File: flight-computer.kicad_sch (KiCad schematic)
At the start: 42 parts, among them J1 MicroSD Slot, J2 USB_C_Receptacle_USB2.0_16P, SW1 SW_Push, SW2 SW_Push, U1 RP2040, U2 W25Q16JVSS, U3 USBLC6-2SC6, Y1 12MHz

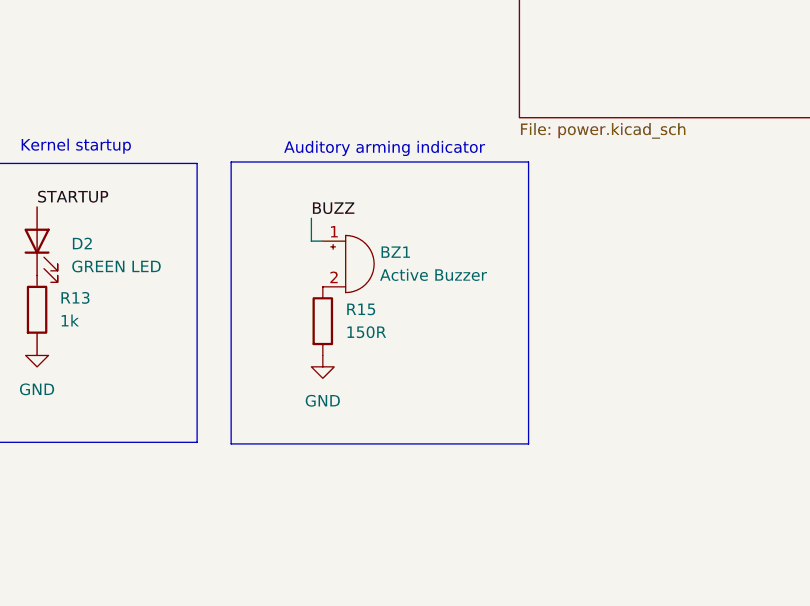
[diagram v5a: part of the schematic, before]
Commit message: Updated PCB so components are now on there.
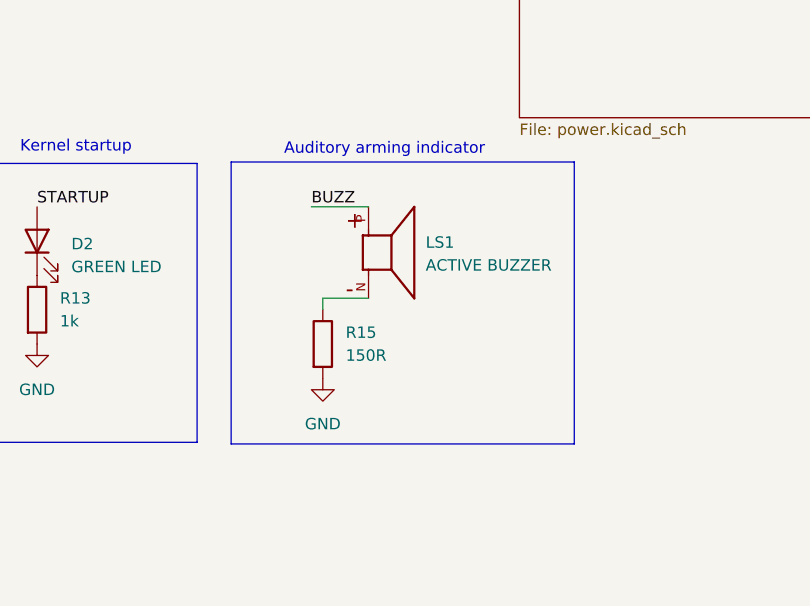
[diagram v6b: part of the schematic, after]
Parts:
- removed BZ1: Active Buzzer, buzzer:XDCR_AI-1223-TWT-3V-2-R, symbol Device:Buzzer
- added LS1: ACTIVE BUZZER, buzzer:XDCR_AI-1223-TWT-3V-2-R, symbol AI-1223-TWT-3V-2-R:AI-1223-TWT-3V-2-R
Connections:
- net BUZZ: now also LS1.P
- net at R15.1: now also LS1.N
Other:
- moved on the sheet: R15
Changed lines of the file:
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@@
 	(wire
 		(pts
+			(xy 322.58 234.95) (xy 317.5 234.95)
+		)
+		(stroke
+			(width 0)
+			(type default)
+		)
+	)
+	(wire
+		(pts
 			(xy 39.37 143.51) (xy 50.8 143.51)
 		)
@@
 	(wire
 		(pts
-			(xy 316.23 226.06) (xy 316.23 228.6)
-		)
-		(stroke
-			(width 0)
-			(type default)
-		)
-	)
-	(wire
-		(pts
 			(xy 72.39 125.73) (xy 60.96 125.73)
 		)
@@
 	(wire
 		(pts
+			(xy 317.5 234.95) (xy 317.5 236.22)
+		)
+		(stroke
+			(width 0)
+			(type default)
+		)
+	)
+	(wire
+		(pts
 			(xy 278.13 68.58) (xy 266.7 68.58)
 		)
@@
 	(wire
 		(pts
-			(xy 316.23 228.6) (xy 317.5 228.6)
+			(xy 316.23 224.79) (xy 322.58 224.79)
 		)
 		(stroke
@@
 	(rectangle
 		(start 307.3134 219.8042)
-		(end 340.36 251.1317)
+		(end 345.44 251.1317)
 		(stroke
 			(width 0)
@@
 	)
 	(label "BUZZ"
-		(at 316.23 226.06 0)
+		(at 316.23 224.79 0)
 		(fields_autoplaced yes)
 		(effects
@@
 	(symbol
 		(lib_id "power:GND")
-		(at 317.5 241.3 0)
+		(at 317.5 243.84 0)
 		(unit 1)
 		(exclude_from_sim no)
@@
 		(fields_autoplaced yes)
 		(property "Reference" "#PWR037"
-			(at 317.5 247.65 0)
+			(at 317.5 250.19 0)
 			(effects
 				(font
@@
 		)
 		(property "Value" "GND"
-			(at 317.5 246.38 0)
+			(at 317.5 248.92 0)
 			(effects
 				(font
@@
 		)
 		(property "Footprint" ""
-			(at 317.5 241.3 0)
+			(at 317.5 243.84 0)
 			(effects
 				(font
@@
 		)
 		(property "Datasheet" ""
-			(at 317.5 241.3 0)
+			(at 317.5 243.84 0)
 			(effects
 				(font
@@
 		)
 		(property "Description" "Power symbol creates a global label with name \"GND\" , ground"
-			(at 317.5 241.3 0)
+			(at 317.5 243.84 0)
 			(effects
 				(font
@@
 	)
 	(symbol
-		(lib_id "Device:Buzzer")
-		(at 320.04 231.14 0)
+		(lib_id "AI-1223-TWT-3V-2-R:AI-1223-TWT-3V-2-R")
+		(at 325.12 229.87 0)
 		(unit 1)
 		(exclude_from_sim no)
@@
 		(dnp no)
 		(fields_autoplaced yes)
-		(property "Reference" "BZ1"
-			(at 323.85 229.8699 0)
+		(property "Reference" "LS1"
+			(at 328.93 228.7442 0)
 			(effects
 				(font
@@
 			)
 		)
-		(property "Value" "Active Buzzer"
-			(at 323.85 232.4099 0)
+		(property "Value" "ACTIVE BUZZER"
+			(at 328.93 231.2842 0)
 			(effects
 				(font
@@
 		)
 		(property "Footprint" "buzzer:XDCR_AI-1223-TWT-3V-2-R"
-			(at 319.405 228.6 90)
+			(at 325.12 229.87 0)
 			(effects
 				(font
 					(size 1.27 1.27)
 				)
+				(justify bottom)
 				(hide yes)
 			)
 		)
-		(property "Datasheet" "~"
-			(at 319.405 228.6 90)
+		(property "Datasheet" ""
+			(at 325.12 229.87 0)
 			(effects
 				(font
@@
 			)
 		)
-		(property "Description" "Buzzer, polarized"
-			(at 320.04 231.14 0)
+		(property "Description" ""
+			(at 325.12 229.87 0)
 			(effects
 				(font
@@
 			)
 		)
-		(pin "1"
+		(property "PARTREV" "3/18/2020"
+			(at 325.12 229.87 0)
+			(effects
+				(font
+					(size 1.27 1.27)
+				)
+				(justify bottom)
+				(hide yes)
+			)
 		)
-		(pin "2"
+		(property "STANDARD" "Manufacturer Recommendations"
+			(at 325.12 229.87 0)
+			(effects
+				(font
+					(size 1.27 1.27)
+				)
+				(justify bottom)
+				(hide yes)
+			)
+		)
+		(property "MAXIMUM_PACKAGE_HEIGHT" "7.8 mm"
+			(at 325.12 229.87 0)
+			(effects
+				(font
+					(size 1.27 1.27)
+				)
+				(justify bottom)
+				(hide yes)
+			)
+		)
+		(property "MANUFACTURER" "PUI Audio"
+			(at 325.12 229.87 0)
+			(effects
+				(font
+					(size 1.27 1.27)
+				)
+				(justify bottom)
+				(hide yes)
+			)
+		)
+		(pin "N"
+		)
+		(pin "P"
 		)
 		(instances
 			(project ""
 				(path "/b90d3133-97a4-4747-8a68-e80f353c7b97"
-					(reference "BZ1")
+					(reference "LS1")
 					(unit 1)
 				)
@@
 	(symbol
 		(lib_id "Device:R")
-		(at 317.5 237.49 0)
+		(at 317.5 240.03 0)
 		(unit 1)
 		(exclude_from_sim no)
@@
 		(fields_autoplaced yes)
 		(property "Reference" "R15"
-			(at 320.04 236.2199 0)
+			(at 320.04 238.7599 0)
 			(effects
 				(font
@@
 		)
 		(property "Value" "150R"
-			(at 320.04 238.7599 0)
+			(at 320.04 241.2999 0)
 			(effects
 				(font
@@
 		)
 		(property "Footprint" "Resistor_SMD:R_0201_0603Metric"
-			(at 315.722 237.49 90)
+			(at 315.722 240.03 90)
 			(effects
 				(font
@@
 		)
 		(property "Datasheet" "~"
-			(at 317.5 237.49 0)
+			(at 317.5 240.03 0)
 			(effects
 				(font
@@
 		)
 		(property "Description" "Resistor"
-			(at 317.5 237.49 0)
+			(at 317.5 240.03 0)
 			(effects
 				(font
